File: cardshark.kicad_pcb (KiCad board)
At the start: 4 copper layers, 237 x 70.4 mm, 81 parts, among them J1 Conn_02x03_Odd_Even, J2 Bus_ISA_8bit, J3 DE15_Receptacle_HighDensity_M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, Q1 MMBT3904, U1 27C256, U10 SN74F260DR, U12 SOJ_256Kx16, U13 SOJ_256Kx16, U2 GD543x_VLB, U3 SOJ_256Kx16, U4 TL431DBZ, U5 KA78M05_TO252, U6 SN74LS245DBR, U7 SOJ_256Kx16, U8 VLB, Y1 CXO_DIP14

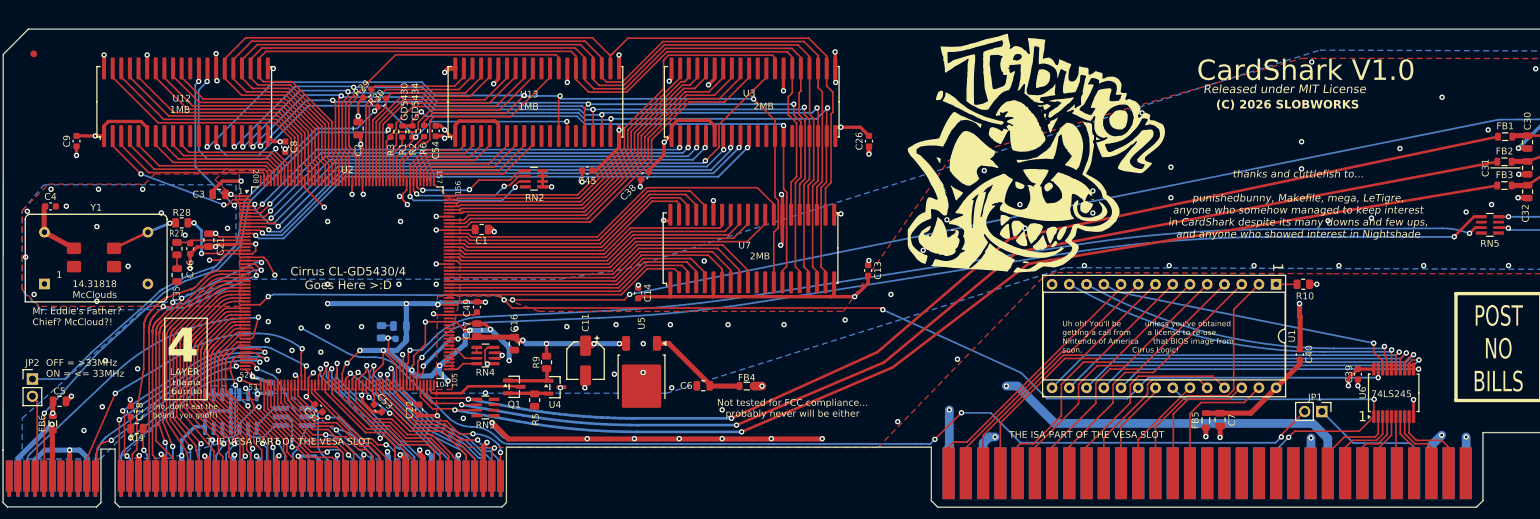
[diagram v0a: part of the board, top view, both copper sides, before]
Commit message: Add files via upload
Updated to v1.1. LOTS of minor tweaks all over.
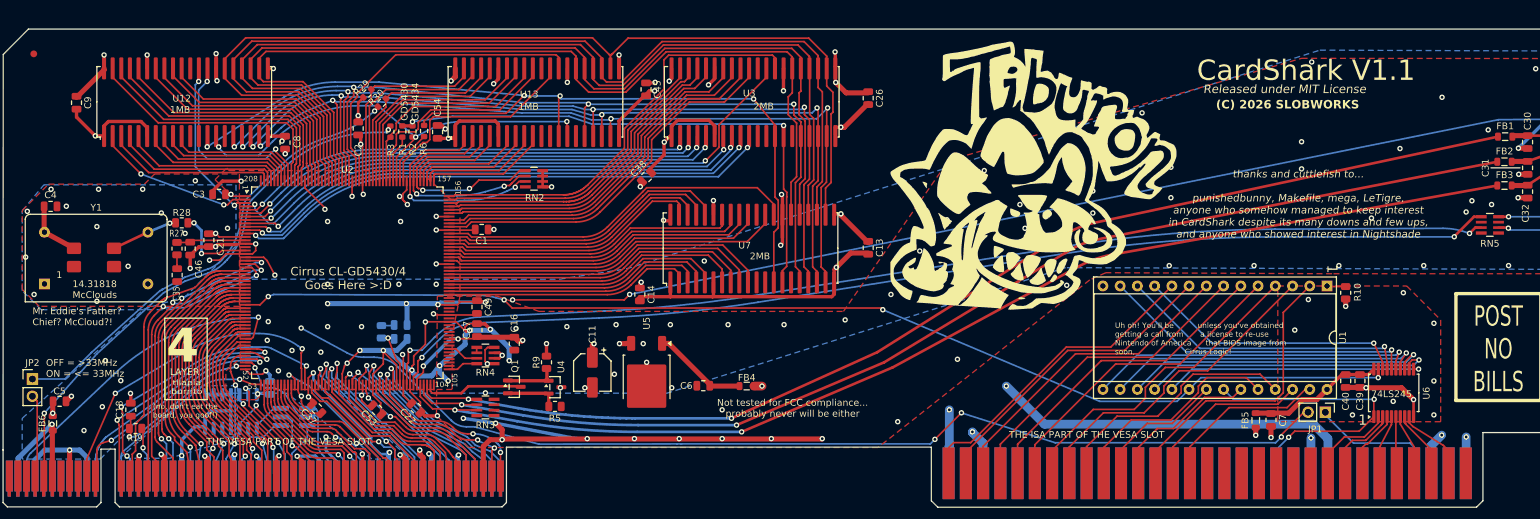
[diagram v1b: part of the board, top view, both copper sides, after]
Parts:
- C13, C14, C18, C19, C22, C26, C37, C38, C39, C4, C40, C44, C45, C46, C49, C53, C54, C8, C9: footprint Capacitor_SMD:C_0603_1608Metric -> Capacitor_SMD:C_0805_2012Metric
- moved C45 14.8 mm to (132.9, 79.0), turned to -90 degrees
- moved C40 7.80 mm to (236.0, 122.0), turned to -90 degrees
- moved C7 7.50 mm to (225.0, 127.8)
- moved U1 7.49 mm to (233.2, 108.0)
- moved FB5 7.35 mm to (222.8, 127.8)
- moved R10 6.37 mm to (236.0, 109.0), turned to -90 degrees
- moved C26 6.34 mm to (165.6, 80.3), turned to -90 degrees
- moved C9 5.66 mm to (49.0, 81.0), turned to -90 degrees
- moved G*** 3.53 mm to (190.6, 92.0)
- moved C13 3.35 mm to (165.6, 102.4)
- moved R5 3.14 mm to (119.5, 125.8), turned to 180 degrees
- moved C11 2.02 mm to (125.0, 120.8)
- moved G*** 1.36 mm to (81.6, 91.5)
- moved C39 1.04 mm to (238.1, 122.0)
- moved U5 0.75 mm to (133.0, 121.5)
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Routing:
- net GND: track 489.5 -> 530.8 mm, vias 172 -> 177
- net /~{SMEMRD}: track 52.8 -> 45.2 mm
- net /BD3: track 56.0 -> 48.5 mm
- net /BD4: track 54.5 -> 47.0 mm
- net /VCC: track 213.5 -> 206.0 mm, vias 21 -> 20
- net /BD5: track 53.0 -> 45.6 mm
- net /BD6: track 50.7 -> 43.3 mm
- net /BD7: track 45.7 -> 38.3 mm
- net /SA0: track 39.5 -> 46.5 mm
- net /SA1: track 39.1 -> 46.1 mm
- net /SA8: track 30.8 -> 37.7 mm
- net /SA9: track 25.3 -> 32.1 mm
- net /SA11: track 15.8 -> 22.4 mm
- net /SA2: track 40.2 -> 46.7 mm
- net /SA7: track 40.8 -> 47.2 mm
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- added copper zone on In2.Cu, net GND
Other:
- board text added: "CardShark V1.1"
- board text removed: "CardShark V1.0"
